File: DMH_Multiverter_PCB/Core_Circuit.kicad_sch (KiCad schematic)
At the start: 16 parts, among them U1 TL072, U2 TL072

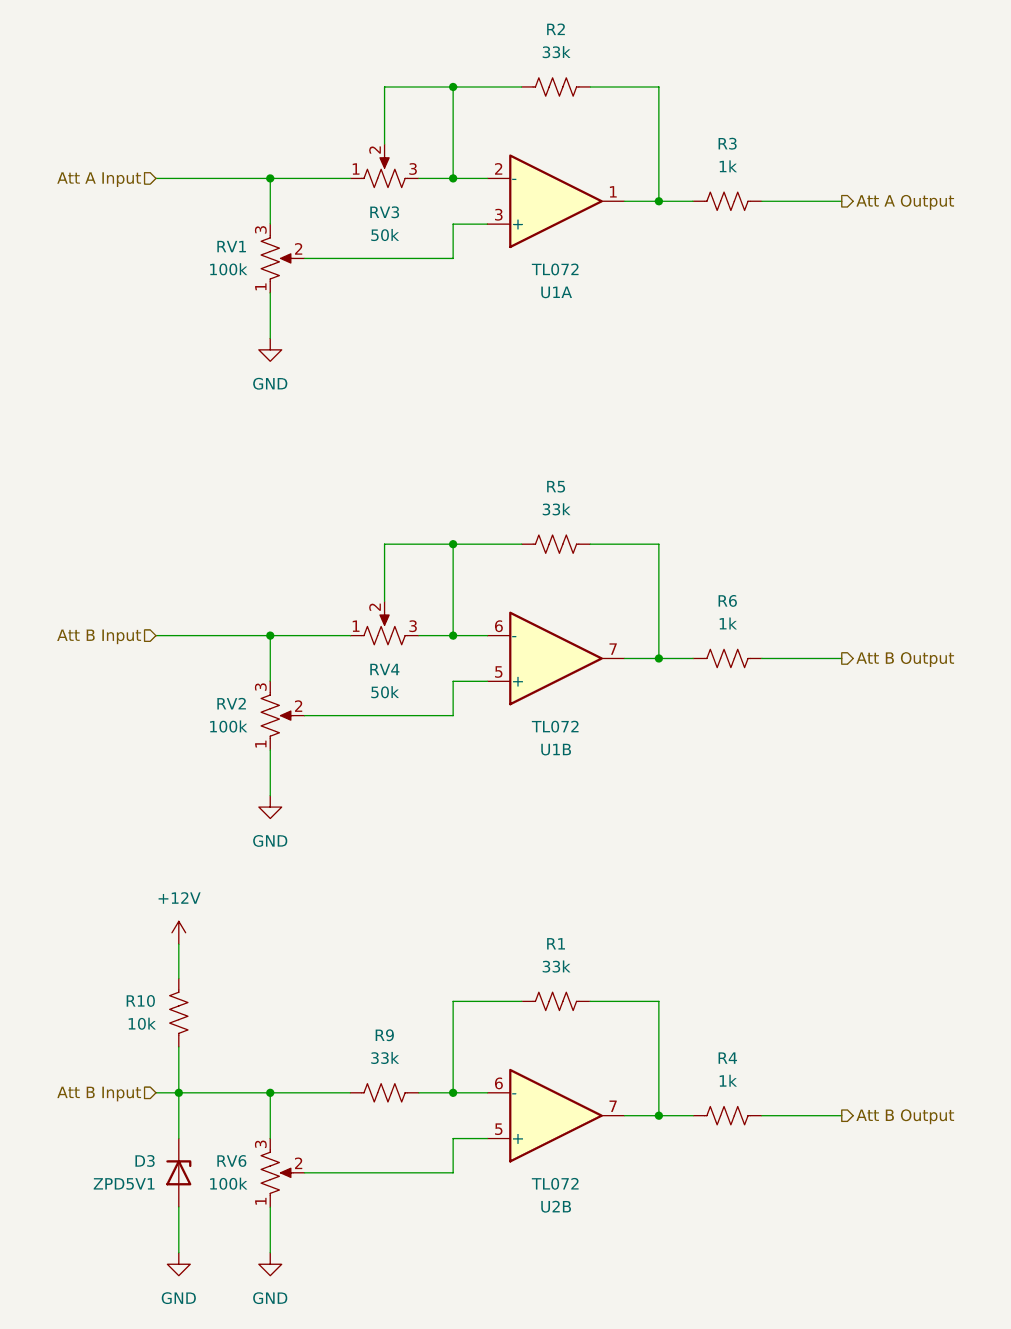
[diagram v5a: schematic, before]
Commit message: Finished Mk2 design
- Changed R7 value to 10k
- Replaced the other resistor with a 5V1 Zener
- Cleaned up schematic
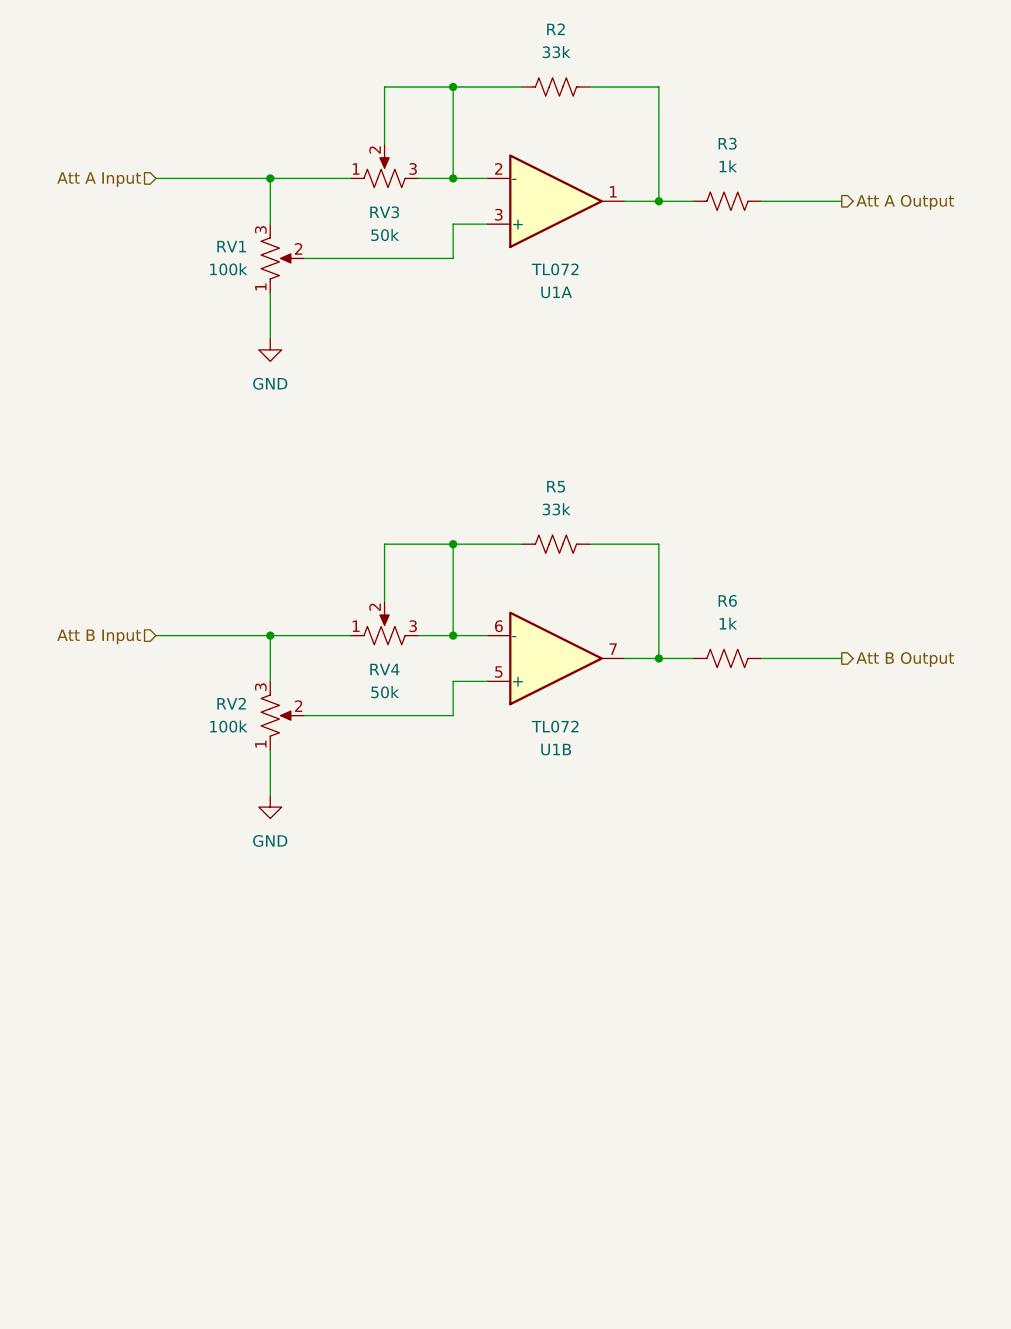
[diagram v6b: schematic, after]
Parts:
- removed D3: ZPD5V1, Diode_THT:D_DO-35_SOD27_P7.62mm_Horizontal, symbol Diode:ZPDxx
- removed R1, R9: 33k, Resistor_THT:R_Axial_DIN0207_L6.3mm_D2.5mm_P7.62mm_Horizontal, symbol Device:R_US
- removed R10: 10k, Resistor_THT:R_Axial_DIN0207_L6.3mm_D2.5mm_P7.62mm_Horizontal, symbol Device:R_US
- removed R4: 1k, Resistor_THT:R_Axial_DIN0207_L6.3mm_D2.5mm_P7.62mm_Horizontal, symbol Device:R_US
- removed RV6: 100k, SynthStuff:Potentiometer_TT_P110KH1, symbol Device:R_Potentiometer_US
- removed U2: TL072, Package_DIP:DIP-8_W7.62mm_Socket, symbol Amplifier_Operational:TL072

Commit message: Switched adjustment trimpots position with Rin
... and renumbered the resistors.
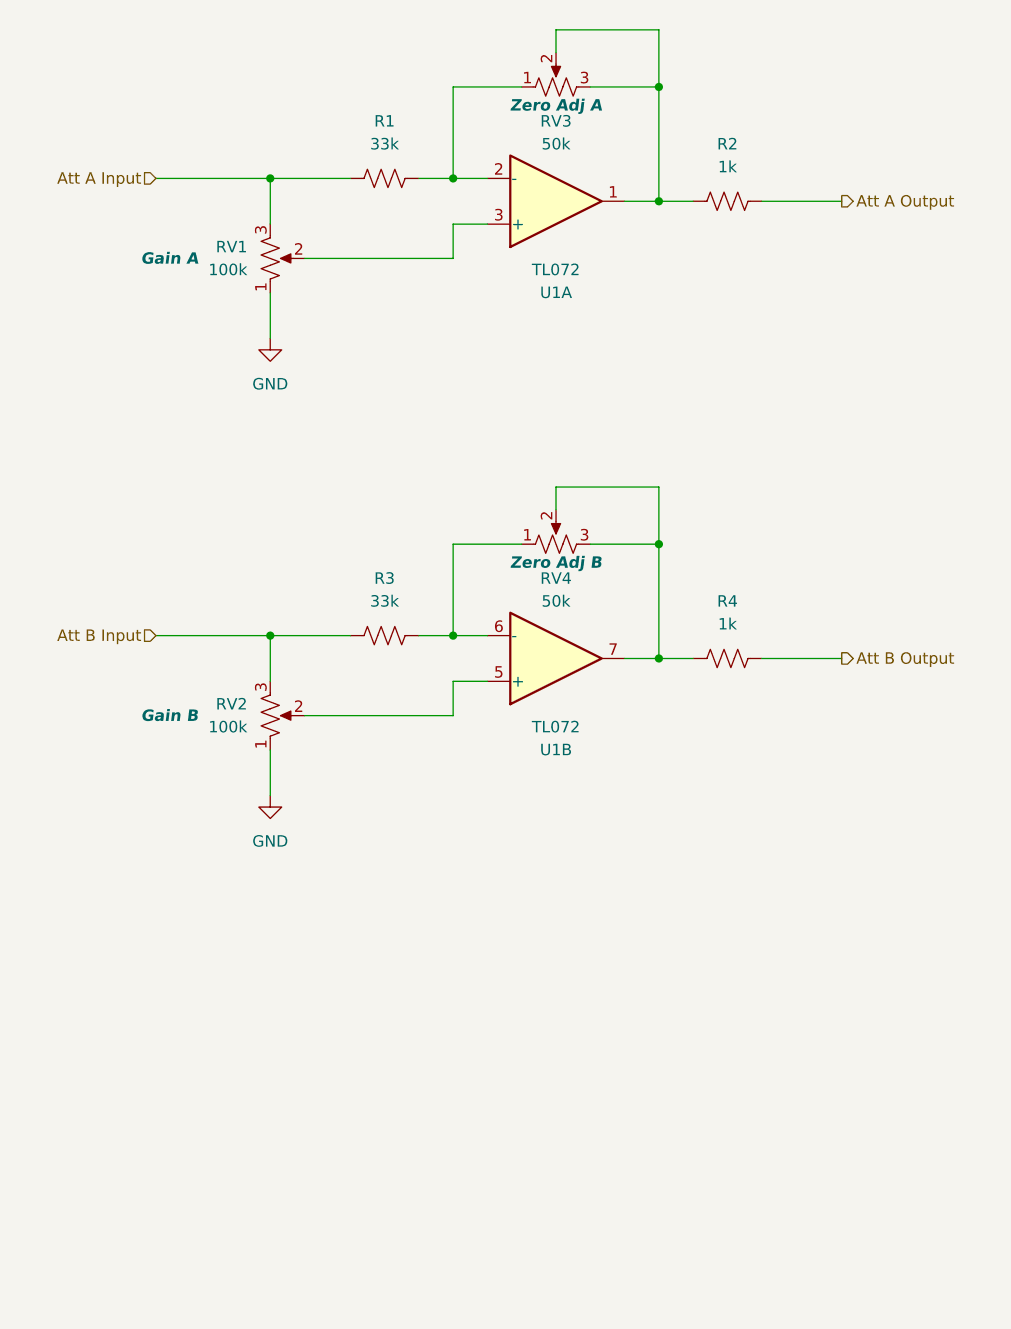
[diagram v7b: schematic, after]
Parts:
- RV1: Function (none) -> Gain A
- RV2: Function (none) -> Gain B
- RV3: Function (none) -> Zero Adj A
- RV4: Function (none) -> Zero Adj B
- renumbered R2 to R1, R3 to R2, R5 to R3, R6 to R4
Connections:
- net Att A Input: now also R1.1; no longer RV3.1
- net Att B Input: now also R3.1; no longer RV4.1
- net at RV4.2, RV4.3: now also R4.1, U1.7; no longer R3.1, U1.6 (-)
- net at RV3.2, RV3.3: now also R2.1, U1.1; no longer R1.1, U1.2 (-)
- new net: R3.2, RV4.1, U1.6 (-)
- new net: R1.2, RV3.1, U1.2 (-)
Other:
- moved on the sheet: R1, R3, RV3, RV4
